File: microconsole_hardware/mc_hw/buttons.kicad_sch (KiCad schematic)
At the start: 33 parts, among them SW10 TL3301NF160QG, SW11 TL3301NF160QG, SW12 TL3301NF160QG, SW13 TL3301NF160QG, SW14 TL3301NF160QG, SW15 TL3301NF160QG, SW16 Joystick, SW17 Joystick, SW2 TL3301NF160QG, SW3 TL3301NF160QG, SW4 TL3301NF160QG, SW5 TL3301NF160QG, SW6 TL3301NF160QG, SW7 TL3301NF160QG, SW8 TL3301NF160QG, SW9 TL3301NF160QG, U3 MCP23017-E/SO, U4 ADS7828E/2K5

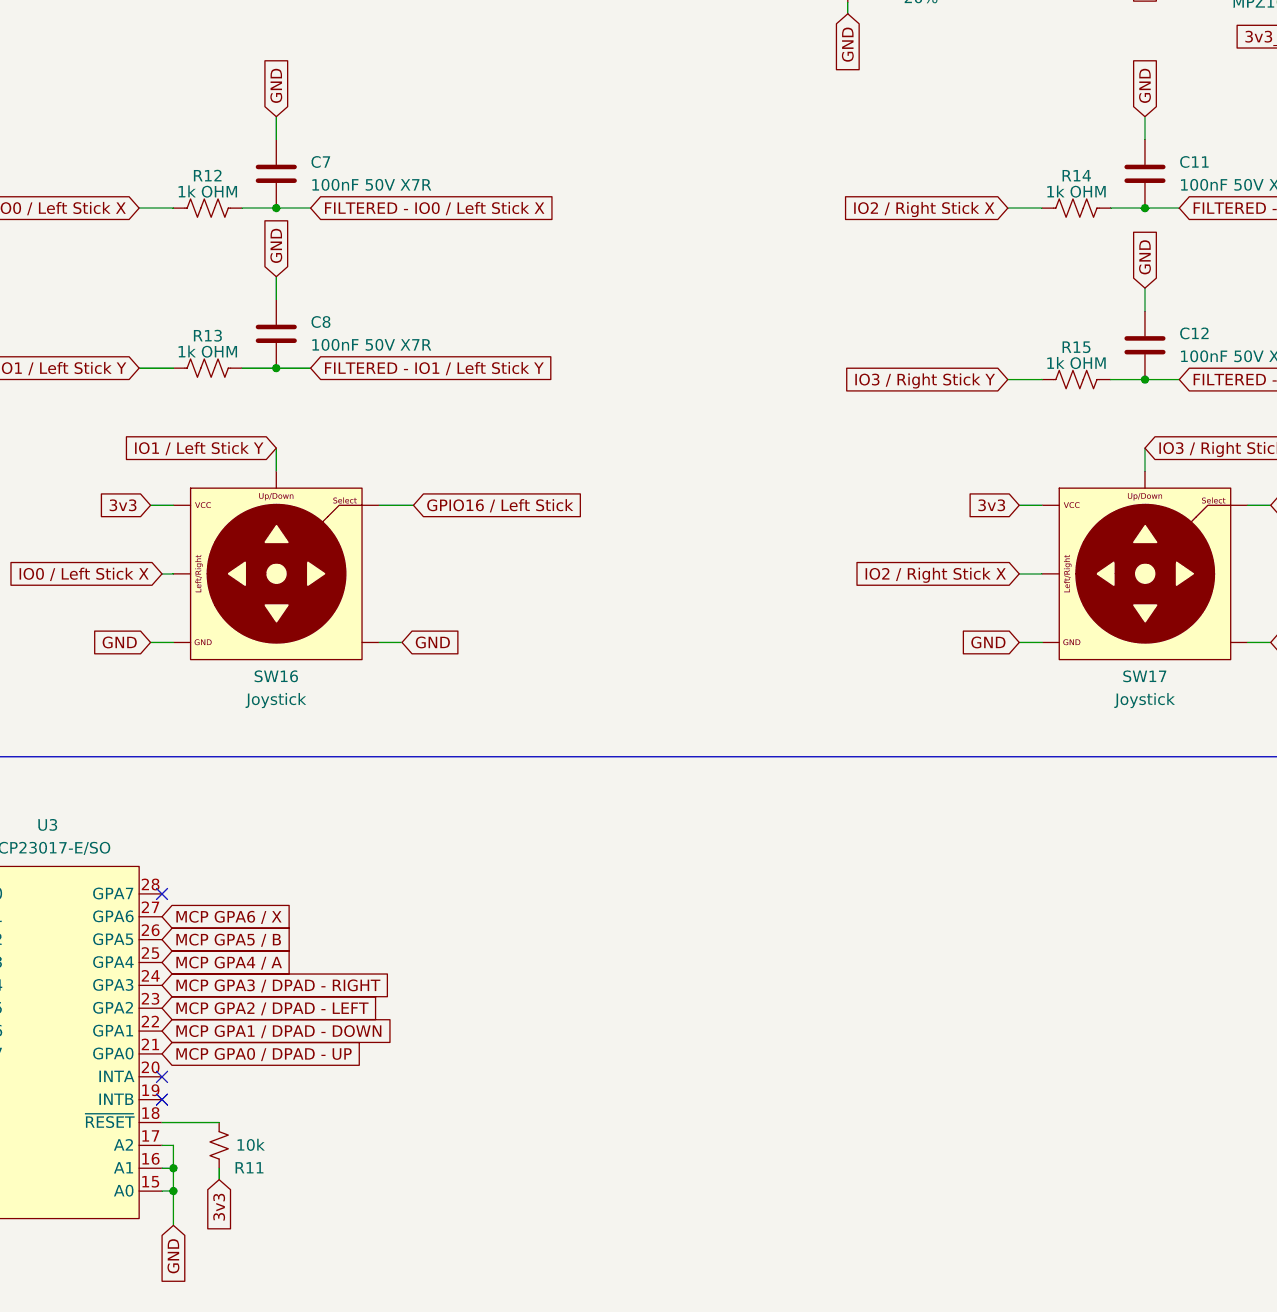
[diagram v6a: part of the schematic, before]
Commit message: resistor and capacitor consolidation.
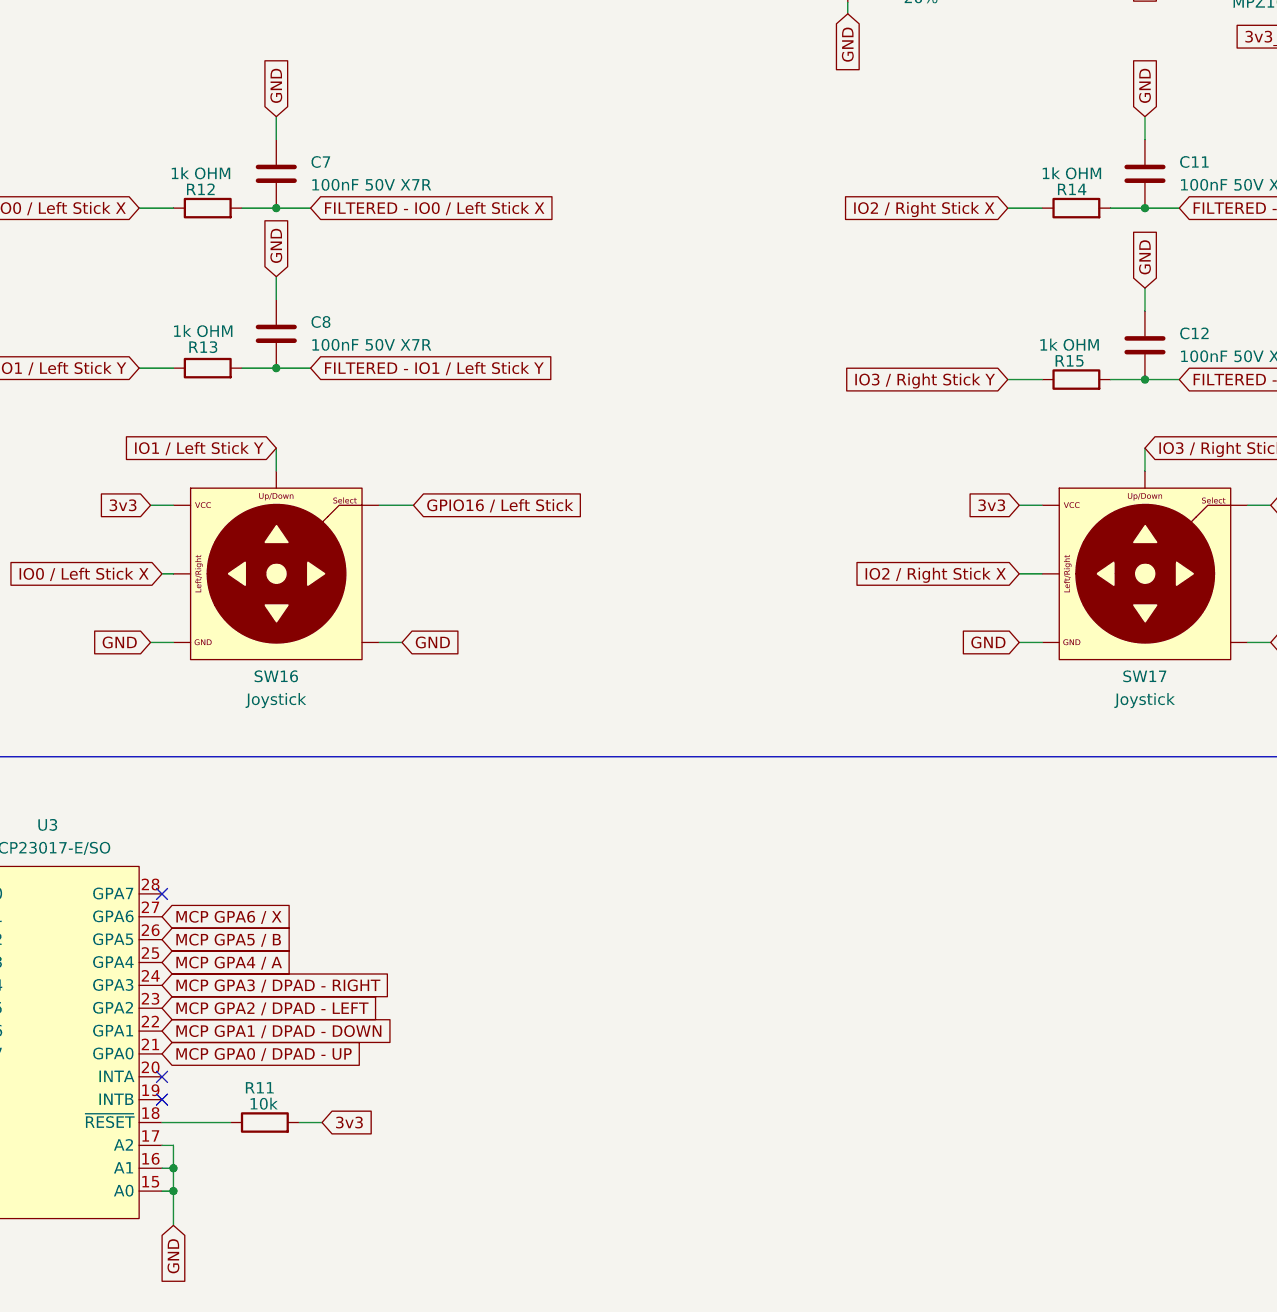
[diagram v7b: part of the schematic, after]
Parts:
- R11: footprint PCM_SparkFun-Resistor:R_0603_1608Metric -> Resistor_SMD:R_0603_1608Metric; symbol PCM_SparkFun-Resistor:0.47_0603 -> Device:R
- R12, R13, R14, R15: footprint PCM_SparkFun-Resistor:R_0603_1608Metric -> Resistor_SMD:R_0603_1608Metric; symbol PCM_SparkFun-Resistor:R -> Device:R
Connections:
- net FILTERED - IO0 / Left Stick X: now also R12.2; no longer R12.1
- net FILTERED - IO1 / Left Stick Y: now also R13.2; no longer R13.1
- net FILTERED - IO2 / Right Stick X: now also R14.2; no longer R14.1
- net FILTERED - IO3 / Right Stick Y: now also R15.2; no longer R15.1
- net IO0 / Left Stick X: now also R12.1; no longer R12.2
- net IO1 / Left Stick Y: now also R13.1; no longer R13.2
- net IO2 / Right Stick X: now also R14.1; no longer R14.2
- net IO3 / Right Stick Y: now also R15.1; no longer R15.2
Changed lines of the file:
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@@
 	(wire
 		(pts
+			(xy 148.59 172.72) (xy 146.05 172.72)
+		)
+		(stroke
+			(width 0)
+			(type default)
+		)
+	)
+	(wire
+		(pts
 			(xy 240.03 60.96) (xy 240.03 63.5)
 		)
@@
 	(wire
 		(pts
-			(xy 137.16 172.72) (xy 130.81 172.72)
+			(xy 138.43 172.72) (xy 130.81 172.72)
 		)
 		(stroke
@@
 	(wire
 		(pts
-			(xy 137.16 179.07) (xy 137.16 177.8)
-		)
-		(stroke
-			(width 0)
-			(type default)
-		)
-	)
-	(wire
-		(pts
 			(xy 87.63 165.1) (xy 77.47 165.1)
 		)
@@
 	(global_label "3v3"
 		(shape input)
-		(at 137.16 179.07 270)
+		(at 148.59 172.72 0)
 		(fields_autoplaced yes)
 		(effects
@@
 				(size 1.27 1.27)
 			)
-			(justify right)
+			(justify left)
 		)
 		(property "Intersheetrefs" "${INTERSHEET_REFS}"
-			(at 137.16 185.4418 90)
+			(at 154.9618 172.72 0)
 			(hide yes)
 			(show_name no)
@@
 					(size 1.27 1.27)
 				)
-				(justify right)
+				(justify left)
 			)
 		)
@@
 	)
 	(symbol
-		(lib_id "PCM_SparkFun-Resistor:R")
-		(at 135.89 71.12 0)
+		(lib_id "Device:R")
+		(at 135.89 71.12 90)
 		(unit 1)
 		(body_style 1)
@@
 		(dnp no)
 		(property "Reference" "R12"
-			(at 135.89 67.564 0)
+			(at 135.128 69.088 90)
 			(show_name no)
 			(do_not_autoplace no)
@@
 		)
 		(property "Value" "1k OHM"
-			(at 135.89 69.342 0)
+			(at 135.128 67.31 90)
 			(show_name no)
 			(do_not_autoplace no)
@@
 			)
 		)
-		(property "Footprint" "PCM_SparkFun-Resistor:R_0603_1608Metric"
-			(at 135.89 75.692 0)
+		(property "Footprint" "Resistor_SMD:R_0603_1608Metric"
+			(at 135.89 72.898 90)
 			(hide yes)
 			(show_name no)
@@
 		)
 		(property "Datasheet" "https://www.vishay.com/docs/20035/dcrcwe3.pdf"
-			(at 134.62 80.01 0)
+			(at 135.89 71.12 0)
 			(hide yes)
 			(show_name no)
@@
 		)
 		(property "Description" "Resistor"
-			(at 135.89 82.55 0)
+			(at 135.89 71.12 0)
 			(hide yes)
 			(show_name no)
@@
 		)
 		(property "PROD_ID" "RES-07856"
-			(at 135.89 77.978 0)
+			(at 142.748 71.12 0)
 			(hide yes)
 			(show_name no)
@@
 	)
 	(symbol
-		(lib_id "PCM_SparkFun-Resistor:0.47_0603")
-		(at 137.16 175.26 270)
+		(lib_id "Device:R")
+		(at 142.24 172.72 90)
 		(unit 1)
 		(body_style 1)
@@
 		(dnp no)
 		(property "Reference" "R11"
-			(at 142.24 177.8 90)
+			(at 139.954 168.91 90)
 			(show_name no)
 			(do_not_autoplace no)
@@
 		)
 		(property "Value" "10k"
-			(at 142.24 175.26 90)
+			(at 140.462 170.688 90)
 			(show_name no)
 			(do_not_autoplace no)
@@
 			)
 		)
-		(property "Footprint" "PCM_SparkFun-Resistor:R_0603_1608Metric"
-			(at 132.588 175.26 0)
+		(property "Footprint" "Resistor_SMD:R_0603_1608Metric"
+			(at 142.24 174.498 90)
 			(hide yes)
 			(show_name no)
@@
 		)
 		(property "Datasheet" "https://industrial.panasonic.com/cdbs/www-data/pdf/RDN0000/AOA0000C313.pdf"
-			(at 128.27 175.26 0)
+			(at 142.24 172.72 0)
 			(hide yes)
 			(show_name no)
@@
 		)
 		(property "Description" "Resistor"
-			(at 125.73 175.26 0)
+			(at 142.24 172.72 0)
 			(hide yes)
 			(show_name no)
@@
 		)
 		(property "PROD_ID" "RES-20715"
-			(at 130.302 175.26 0)
+			(at 149.098 172.72 0)
 			(hide yes)
 			(show_name no)
@@
 	)
 	(symbol
-		(lib_id "PCM_SparkFun-Resistor:R")
-		(at 232.41 90.17 0)
+		(lib_id "Device:R")
+		(at 232.41 90.17 90)
 		(unit 1)
 		(body_style 1)
@@
 		(dnp no)
 		(property "Reference" "R15"
-			(at 232.41 86.614 0)
+			(at 231.648 88.138 90)
 			(show_name no)
 			(do_not_autoplace no)
@@
 		)
 		(property "Value" "1k OHM"
-			(at 232.41 88.392 0)
+			(at 231.648 86.36 90)
 			(show_name no)
 			(do_not_autoplace no)
@@
 			)
 		)
-		(property "Footprint" "PCM_SparkFun-Resistor:R_0603_1608Metric"
-			(at 232.41 94.742 0)
+		(property "Footprint" "Resistor_SMD:R_0603_1608Metric"
+			(at 232.41 91.948 90)
 			(hide yes)
 			(show_name no)
@@
 		)
 		(property "Datasheet" "https://www.vishay.com/docs/20035/dcrcwe3.pdf"
-			(at 231.14 99.06 0)
+			(at 232.41 90.17 0)
 			(hide yes)
 			(show_name no)
@@
 		)
 		(property "Description" "Resistor"
-			(at 232.41 101.6 0)
+			(at 232.41 90.17 0)
 			(hide yes)
 			(show_name no)
@@
 		)
 		(property "PROD_ID" "RES-07856"
-			(at 232.41 97.028 0)
+			(at 239.268 90.17 0)
 			(hide yes)
 			(show_name no)
@@
 	)
 	(symbol
-		(lib_id "PCM_SparkFun-Resistor:R")
-		(at 232.41 71.12 0)
+		(lib_id "Device:R")
+		(at 232.41 71.12 90)
 		(unit 1)
 		(body_style 1)
@@
 		(dnp no)
 		(property "Reference" "R14"
-			(at 232.41 67.564 0)
+			(at 231.902 69.088 90)
 			(show_name no)
 			(do_not_autoplace no)
@@
 		)
 		(property "Value" "1k OHM"
-			(at 232.41 69.342 0)
+			(at 231.902 67.31 90)
 			(show_name no)
 			(do_not_autoplace no)
@@
 			)
 		)
-		(property "Footprint" "PCM_SparkFun-Resistor:R_0603_1608Metric"
-			(at 232.41 75.692 0)
+		(property "Footprint" "Resistor_SMD:R_0603_1608Metric"
+			(at 232.41 72.898 90)
 			(hide yes)
 			(show_name no)
@@
 		)
 		(property "Datasheet" "https://www.vishay.com/docs/20035/dcrcwe3.pdf"
-			(at 231.14 80.01 0)
+			(at 232.41 71.12 0)
 			(hide yes)
 			(show_name no)
@@
 		)
 		(property "Description" "Resistor"
-			(at 232.41 82.55 0)
+			(at 232.41 71.12 0)
 			(hide yes)
 			(show_name no)
@@
 		)
 		(property "PROD_ID" "RES-07856"
-			(at 232.41 77.978 0)
+			(at 239.268 71.12 0)
 			(hide yes)
 			(show_name no)
@@
 	)
 	(symbol
-		(lib_id "PCM_SparkFun-Resistor:R")
-		(at 135.89 88.9 0)
+		(lib_id "Device:R")
+		(at 135.89 88.9 90)
 		(unit 1)
 		(body_style 1)
@@
 		(dnp no)
 		(property "Reference" "R13"
-			(at 135.89 85.344 0)
+			(at 135.382 86.614 90)
 			(show_name no)
 			(do_not_autoplace no)
@@
 		)
 		(property "Value" "1k OHM"
-			(at 135.89 87.122 0)
+			(at 135.382 84.836 90)
 			(show_name no)
 			(do_not_autoplace no)
@@
 			)
 		)
-		(property "Footprint" "PCM_SparkFun-Resistor:R_0603_1608Metric"
-			(at 135.89 93.472 0)
+		(property "Footprint" "Resistor_SMD:R_0603_1608Metric"
+			(at 135.89 90.678 90)
 			(hide yes)
 			(show_name no)
@@
 		)
 		(property "Datasheet" "https://www.vishay.com/docs/20035/dcrcwe3.pdf"
-			(at 134.62 97.79 0)
+			(at 135.89 88.9 0)
 			(hide yes)
 			(show_name no)
@@
 		)
 		(property "Description" "Resistor"
-			(at 135.89 100.33 0)
+			(at 135.89 88.9 0)
 			(hide yes)
 			(show_name no)
@@
 		)
 		(property "PROD_ID" "RES-07856"
-			(at 135.89 95.758 0)
+			(at 142.748 88.9 0)
 			(hide yes)
 			(show_name no)

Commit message: cleanup caps and resistors
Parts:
- C9: footprint PCM_SparkFun-Capacitor:C_0805_2012Metric -> Capacitor_SMD:C_0805_2012Metric
- R12, R13, R14, R15: value 1k OHM -> 1k
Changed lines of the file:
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@@
 			)
 		)
-		(property "Value" "1k OHM"
+		(property "Value" "1k"
 			(at 135.128 67.31 90)
 			(show_name no)
@@
 			)
 		)
-		(property "Footprint" "PCM_SparkFun-Capacitor:C_0805_2012Metric"
+		(property "Footprint" "Capacitor_SMD:C_0805_2012Metric"
 			(at 207.01 57.15 0)
 			(hide yes)
@@
 			)
 		)
-		(property "Value" "1k OHM"
+		(property "Value" "1k"
 			(at 231.648 86.36 90)
 			(show_name no)
@@
 			)
 		)
-		(property "Value" "1k OHM"
+		(property "Value" "1k"
 			(at 231.902 67.31 90)
 			(show_name no)
@@
 			)
 		)
-		(property "Value" "1k OHM"
+		(property "Value" "1k"
 			(at 135.382 84.836 90)
 			(show_name no)
